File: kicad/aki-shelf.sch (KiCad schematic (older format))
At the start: 39 parts, among them SW1 RESET, SW10 2x2, SW11 2x3, SW12 1x1, SW13 1x2, SW14 1x3, SW2 UPLOAD, SW3 4x1, SW4 4x2, SW5 4x3, SW6 3x1, SW7 3x2, SW8 3x3, SW9 2x1, U1 NJM2884, U2 AE-FT234X, U3 OPA344NA, U4 AQM0802, U5 ESP-WROOM-32

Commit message: 自動配線を適用
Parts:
- LS1: value Speaker -> UGCT7525AN4
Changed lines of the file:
@@
 LIBS:aki-shelf
 LIBS:switches
+LIBS:aki-shelf-cache
 EELAYER 25 0
 EELAYER END
@@
 P 6450 3200
 F 0 "LS1" H 6500 3425 50  0000 R CNN
-F 1 "Speaker" H 6500 3350 50  0000 R CNN
+F 1 "UGCT7525AN4" H 6500 3350 50  0000 R CNN
 F 2 "aki-shelf:UGCT7525AN4" H 6450 3000 50  0001 C CNN
 F 3 "" H 6440 3150 50  0001 C CNN

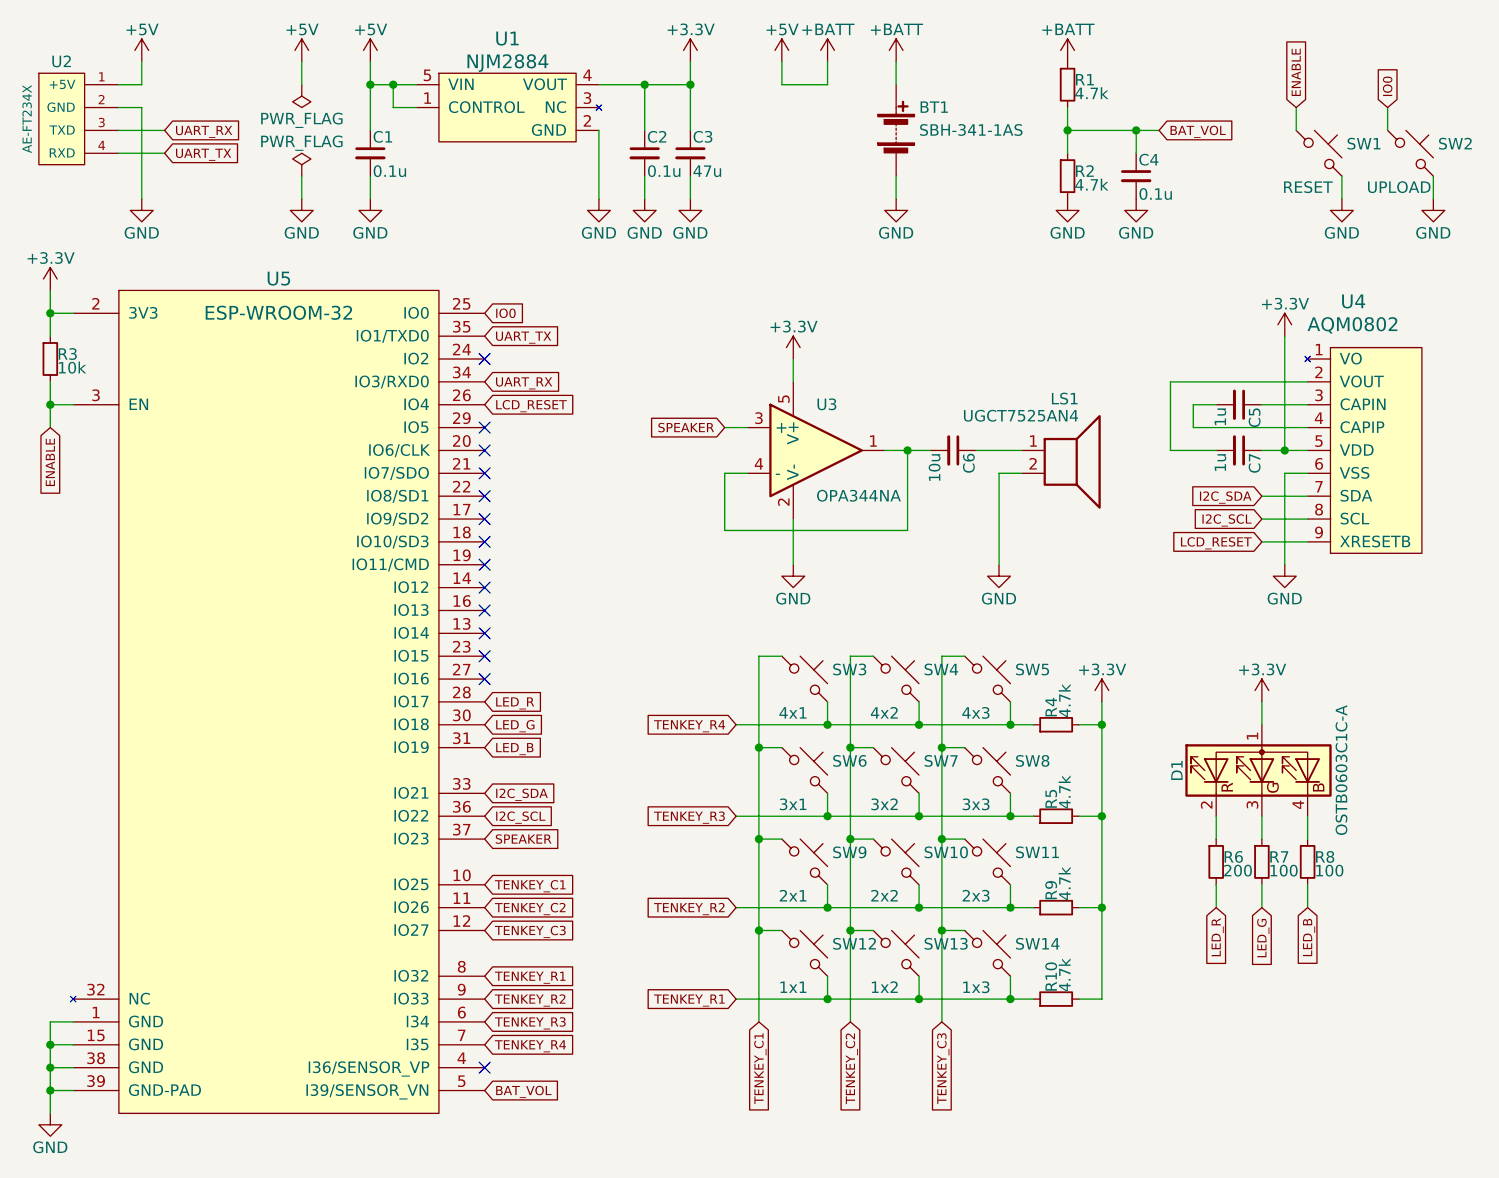
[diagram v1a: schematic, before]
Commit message: 基板を両面にして小型化
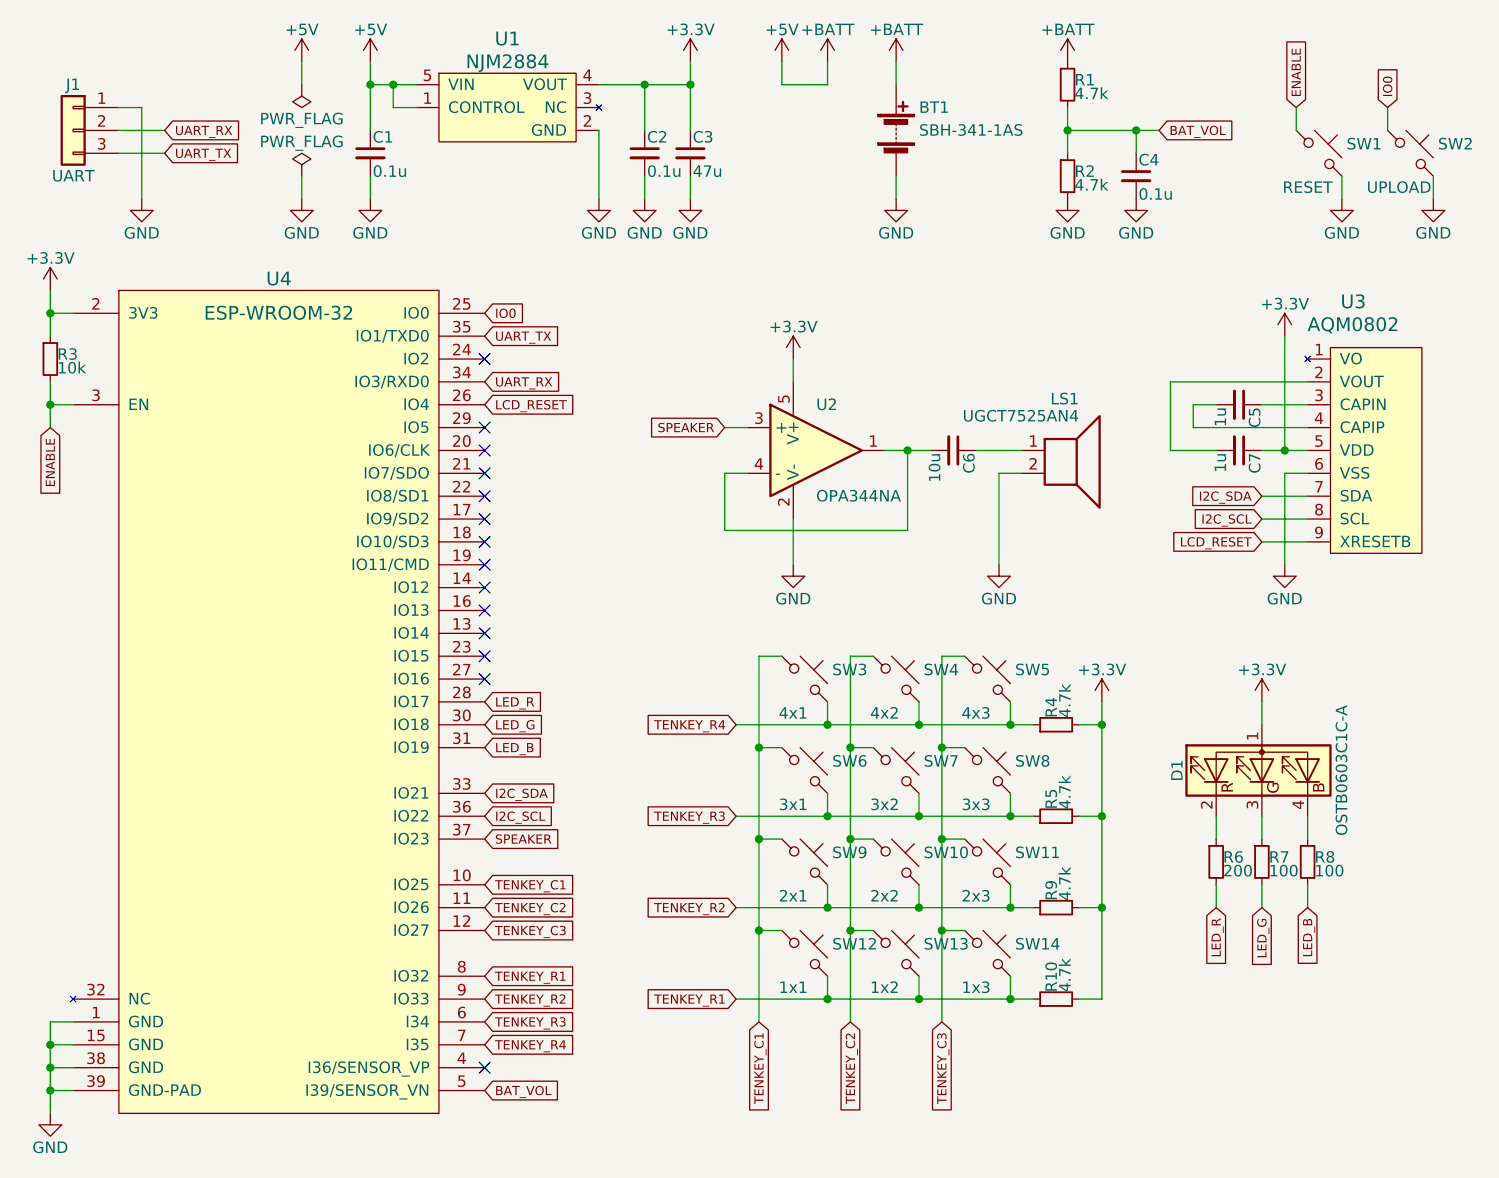
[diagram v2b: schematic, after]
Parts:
- removed U2: AE-FT234X, Pin_Headers:Pin_Header_Straight_1x04_Pitch2.54mm, symbol AE-FT234X
- added J1: UART, Socket_Strips:Socket_Strip_Straight_1x03_Pitch2.54mm, symbol Conn_01x03
- renumbered U3 to U2, U4 to U3, U5 to U4
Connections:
- net GND: now also J1.1 (Pin_1)
- net UART_RX: now also J1.2 (Pin_2)
- net UART_TX: now also J1.3 (Pin_3)
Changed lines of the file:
@@
 	8050 2100 8050 2000
 $Comp
-L OPA340NA U3
+L OPA340NA U2
 U 1 1 5A899835
 P 5350 3200
-F 0 "U3" H 5350 3400 50  0000 L CNN
+F 0 "U2" H 5350 3400 50  0000 L CNN
 F 1 "OPA344NA" H 5350 3000 50  0000 L CNN
 F 2 "TO_SOT_Packages_SMD:SOT-23-5" H 5350 3200 50  0001 C CNN
@@
 $EndComp
 $Comp
-L AQM0802 U4
+L AQM0802 U3
 U 1 1 5A8C4AD2
 P 7700 3200
-F 0 "U4" H 7700 3850 60  0000 C CNN
+F 0 "U3" H 7700 3850 60  0000 C CNN
 F 1 "AQM0802" H 7700 3750 60  0000 C CNN
 F 2 "aki-shelf:AQM0802A-RN-GBW" H 7700 3750 60  0001 C CNN
@@
 $EndComp
 Wire Wire Line
-	2400 1600 2300 1600
-Wire Wire Line
-	2400 1600 2400 1500
-$Comp
-L +5V #PWR022
-U 1 1 58F006DB
-P 2400 1500
-F 0 "#PWR022" H 2400 1350 50  0001 C CNN
-F 1 "+5V" H 2400 1640 50  0000 C CNN
-F 2 "" H 2400 1500 50  0000 C CNN
-F 3 "" H 2400 1500 50  0000 C CNN
-	1    2400 1500
-	1    0    0    -1
-$EndComp
-Wire Wire Line
 	5700 1500 5700 1600
 $Comp
@@
 $EndComp
 $Comp
-L AE-FT234X U2
-U 1 1 5A8AD757
-P 2100 1750
-F 0 "U2" H 2050 2000 50  0000 C CNN
-F 1 "AE-FT234X" V 1900 1750 40  0000 C CNN
-F 2 "Pin_Headers:Pin_Header_Straight_1x04_Pitch2.54mm" H 2100 2200 60  0001 C CNN
-F 3 "" H 2100 2200 60  0000 C CNN
-	1    2100 1750
-	1    0    0    -1
-$EndComp
-$Comp
-L ESP-WROOM-32 U5
+L ESP-WROOM-32 U4
 U 1 1 5A8AD7EC
 P 3000 4000
-F 0 "U5" H 3000 5550 60  0000 C CNN
+F 0 "U4" H 3000 5550 60  0000 C CNN
 F 1 "ESP-WROOM-32" H 3000 5400 60  0000 C CNN
 F 2 "aki-shelf:ESP-WROOM-32" H 3000 5500 60  0001 C CNN
@@
 NoConn ~ 3900 5900
 $Comp
-L PWR_FLAG #FLG023
+L PWR_FLAG #FLG022
 U 1 1 5A8AC441
 P 3100 1600
-F 0 "#FLG023" H 3100 1675 50  0001 C CNN
+F 0 "#FLG022" H 3100 1675 50  0001 C CNN
 F 1 "PWR_FLAG" H 3100 1750 50  0000 C CNN
 F 2 "" H 3100 1600 50  0001 C CNN
@@
 $EndComp
 $Comp
-L +5V #PWR024
+L +5V #PWR023
 U 1 1 5A8AC4CB
 P 3100 1500
-F 0 "#PWR024" H 3100 1350 50  0001 C CNN
+F 0 "#PWR023" H 3100 1350 50  0001 C CNN
 F 1 "+5V" H 3100 1640 50  0000 C CNN
 F 2 "" H 3100 1500 50  0000 C CNN
@@
 	3100 1500 3100 1600
 $Comp
-L GND #PWR025
+L GND #PWR024
 U 1 1 5A8AC606
 P 3100 2100
-F 0 "#PWR025" H 3100 1850 50  0001 C CNN
+F 0 "#PWR024" H 3100 1850 50  0001 C CNN
 F 1 "GND" H 3100 1950 50  0000 C CNN
 F 2 "" H 3100 2100 50  0000 C CNN
@@
 $EndComp
 $Comp
-L PWR_FLAG #FLG026
+L PWR_FLAG #FLG025
 U 1 1 5A8AC689
 P 3100 2000
-F 0 "#FLG026" H 3100 2075 50  0001 C CNN
+F 0 "#FLG025" H 3100 2075 50  0001 C CNN
 F 1 "PWR_FLAG" H 3100 2150 50  0000 C CNN
 F 2 "" H 3100 2000 50  0001 C CNN
@@
 	3100 2000 3100 2100
 $Comp
-L +BATT #PWR027
+L +BATT #PWR026
 U 1 1 5A8B177B
 P 5700 1500
-F 0 "#PWR027" H 5700 1350 50  0001 C CNN
+F 0 "#PWR026" H 5700 1350 50  0001 C CNN
 F 1 "+BATT" H 5700 1640 50  0000 C CNN
 F 2 "" H 5700 1500 50  0001 C CNN
@@
 $EndComp
 $Comp
-L +BATT #PWR028
+L +BATT #PWR027
 U 1 1 5A8B1853
 P 6450 1500
-F 0 "#PWR028" H 6450 1350 50  0001 C CNN
+F 0 "#PWR027" H 6450 1350 50  0001 C CNN
 F 1 "+BATT" H 6450 1640 50  0000 C CNN
 F 2 "" H 6450 1500 50  0001 C CNN
@@
 $EndComp
 $Comp
-L +5V #PWR029
+L +5V #PWR028
 U 1 1 5A8B1ED8
 P 5200 1500
-F 0 "#PWR029" H 5200 1350 50  0001 C CNN
+F 0 "#PWR028" H 5200 1350 50  0001 C CNN
 F 1 "+5V" H 5200 1640 50  0000 C CNN
 F 2 "" H 5200 1500 50  0000 C CNN
@@
 $EndComp
 $Comp
-L +BATT #PWR030
+L +BATT #PWR029
 U 1 1 5A8B1F58
 P 5400 1500
-F 0 "#PWR030" H 5400 1350 50  0001 C CNN
+F 0 "#PWR029" H 5400 1350 50  0001 C CNN
 F 1 "+BATT" H 5400 1640 50  0000 C CNN
 F 2 "" H 5400 1500 50  0001 C CNN
@@
 Wire Wire Line
 	5400 1600 5400 1500
+$Comp
+L Conn_01x03 J1
+U 1 1 5A8E4B4D
+P 2100 1800
+F 0 "J1" H 2100 2000 50  0000 C CNN
+F 1 "UART" H 2100 1600 50  0000 C CNN
+F 2 "Socket_Strips:Socket_Strip_Straight_1x03_Pitch2.54mm" H 2100 1800 50  0001 C CNN
+F 3 "" H 2100 1800 50  0001 C CNN
+	1    2100 1800
+	-1   0    0    -1
+$EndComp
 $EndSCHEMATC

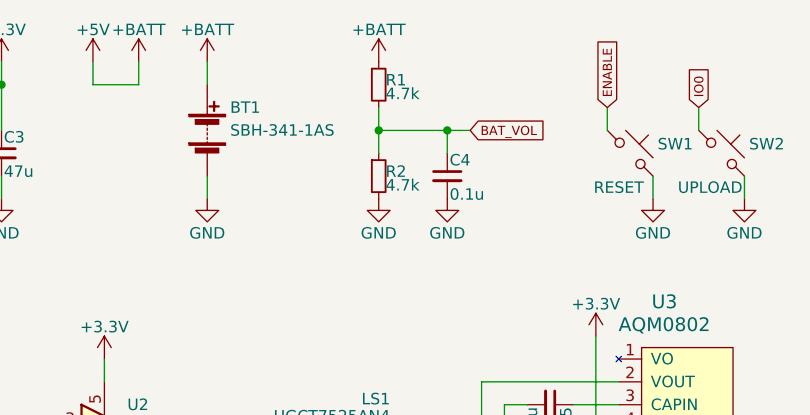
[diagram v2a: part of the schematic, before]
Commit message: 穴径を3mmに変更
貼り付けボスが使えるように
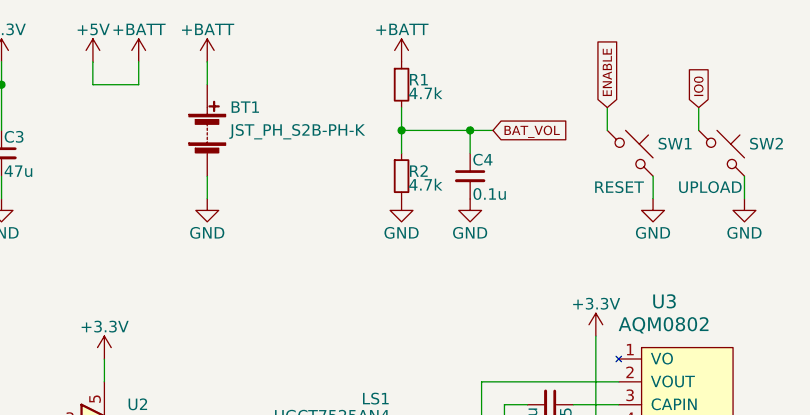
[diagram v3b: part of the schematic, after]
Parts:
- BT1: value SBH-341-1AS -> JST_PH_S2B-PH-K
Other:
- moved on the sheet: C4, R1, R2
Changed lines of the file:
@@
 P 5700 1800
 F 0 "BT1" H 5800 1900 50  0000 L CNN
-F 1 "SBH-341-1AS" H 5800 1800 50  0000 L CNN
+F 1 "JST_PH_S2B-PH-K" H 5800 1800 50  0000 L CNN
 F 2 "Connectors_JST:JST_PH_S2B-PH-K_02x2.00mm_Angled" V 5700 1860 50  0001 C CNN
 F 3 "" V 5700 1860 50  0001 C CNN
@@
 L R_Small R1
 U 1 1 5A8D8861
-P 6450 1600
-F 0 "R1" H 6480 1620 50  0000 L CNN
-F 1 "4.7k" H 6480 1560 50  0000 L CNN
-F 2 "Resistors_SMD:R_0603" H 6450 1600 50  0001 C CNN
-F 3 "" H 6450 1600 50  0001 C CNN
-	1    6450 1600
+P 6550 1600
+F 0 "R1" H 6580 1620 50  0000 L CNN
+F 1 "4.7k" H 6580 1560 50  0000 L CNN
+F 2 "Resistors_SMD:R_0603" H 6550 1600 50  0001 C CNN
+F 3 "" H 6550 1600 50  0001 C CNN
+	1    6550 1600
 	1    0    0    -1
 $EndComp
@@
 L R_Small R2
 U 1 1 5A8D88EB
-P 6450 2000
-F 0 "R2" H 6480 2020 50  0000 L CNN
-F 1 "4.7k" H 6480 1960 50  0000 L CNN
-F 2 "Resistors_SMD:R_0603" H 6450 2000 50  0001 C CNN
-F 3 "" H 6450 2000 50  0001 C CNN
-	1    6450 2000
+P 6550 2000
+F 0 "R2" H 6580 2020 50  0000 L CNN
+F 1 "4.7k" H 6580 1960 50  0000 L CNN
+F 2 "Resistors_SMD:R_0603" H 6550 2000 50  0001 C CNN
+F 3 "" H 6550 2000 50  0001 C CNN
+	1    6550 2000
 	1    0    0    -1
 $EndComp
@@
 L GND #PWR014
 U 1 1 5A8D8D69
-P 6450 2100
-F 0 "#PWR014" H 6450 1850 50  0001 C CNN
-F 1 "GND" H 6450 1950 50  0000 C CNN
-F 2 "" H 6450 2100 50  0000 C CNN
-F 3 "" H 6450 2100 50  0000 C CNN
-	1    6450 2100
+P 6550 2100
+F 0 "#PWR014" H 6550 1850 50  0001 C CNN
+F 1 "GND" H 6550 1950 50  0000 C CNN
+F 2 "" H 6550 2100 50  0000 C CNN
+F 3 "" H 6550 2100 50  0000 C CNN
+	1    6550 2100
 	1    0    0    -1
 $EndComp
@@
 L C_Small C4
 U 1 1 5A8D8E3E
-P 6750 2000
-F 0 "C4" H 6760 2070 50  0000 L CNN
-F 1 "0.1u" H 6760 1920 50  0000 L CNN
-F 2 "Capacitors_SMD:C_0603" H 6750 2000 50  0001 C CNN
-F 3 "" H 6750 2000 50  0001 C CNN
-	1    6750 2000
+P 6850 2000
+F 0 "C4" H 6860 2070 50  0000 L CNN
+F 1 "0.1u" H 6860 1920 50  0000 L CNN
+F 2 "Capacitors_SMD:C_0603" H 6850 2000 50  0001 C CNN
+F 3 "" H 6850 2000 50  0001 C CNN
+	1    6850 2000
 	1    0    0    -1
 $EndComp
@@
 L GND #PWR015
 U 1 1 5A8D8F7F
-P 6750 2100
-F 0 "#PWR015" H 6750 1850 50  0001 C CNN
-F 1 "GND" H 6750 1950 50  0000 C CNN
-F 2 "" H 6750 2100 50  0000 C CNN
-F 3 "" H 6750 2100 50  0000 C CNN
-	1    6750 2100
-	1    0    0    -1
-$EndComp
-Wire Wire Line
-	6750 1900 6750 1800
-Wire Wire Line
-	6450 1800 6850 1800
-Wire Wire Line
-	6450 1700 6450 1900
-Connection ~ 6450 1800
-Text GLabel 6850 1800 2    40   Input ~ 0
+P 6850 2100
+F 0 "#PWR015" H 6850 1850 50  0001 C CNN
+F 1 "GND" H 6850 1950 50  0000 C CNN
+F 2 "" H 6850 2100 50  0000 C CNN
+F 3 "" H 6850 2100 50  0000 C CNN
+	1    6850 2100
+	1    0    0    -1
+$EndComp
+Wire Wire Line
+	6850 1900 6850 1800
+Wire Wire Line
+	6550 1800 6950 1800
+Wire Wire Line
+	6550 1700 6550 1900
+Connection ~ 6550 1800
+Text GLabel 6950 1800 2    40   Input ~ 0
 BAT_VOL
-Connection ~ 6750 1800
+Connection ~ 6850 1800
 Wire Wire Line
 	3400 2000 3400 2100
@@
 L +BATT #PWR027
 U 1 1 5A8B1853
-P 6450 1500
-F 0 "#PWR027" H 6450 1350 50  0001 C CNN
-F 1 "+BATT" H 6450 1640 50  0000 C CNN
-F 2 "" H 6450 1500 50  0001 C CNN
-F 3 "" H 6450 1500 50  0001 C CNN
-	1    6450 1500
-	1    0    0    -1
-$EndComp
+P 6550 1500
+F 0 "#PWR027" H 6550 1350 50  0001 C CNN
+F 1 "+BATT" H 6550 1640 50  0000 C CNN
+F 2 "" H 6550 1500 50  0001 C CNN
+F 3 "" H 6550 1500 50  0001 C CNN
+	1    6550 1500
+	1    0    0    -1
+$EndComp

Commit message: 基板を改良
スイッチの位置，スピーカーの回路など
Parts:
- removed C6: 10u, Capacitors_SMD:C_0805, symbol C_Small
- removed D1: OSTB0603C1C-A, aki-shelf:OSTB0603C1C-A, symbol LED_ARGB
- removed U2: OPA344NA, TO_SOT_Packages_SMD:SOT-23-5, symbol OPA340NA
- added C7: 0.1u, Capacitors_SMD:C_0603, symbol C_Small
- added D1: OSTB0603C1C-A, aki-shelf:OSTB0603C1C-A, symbol OSTB0603C1C-A
- added Q1: BSS138, TO_SOT_Packages_SMD:SOT-23, symbol Q_NMOS_GSD
- added R4: 100k, Resistors_SMD:R_0603, symbol R_Small
- R3: value 10k -> 4.7k
- renumbered C7 to C6, R9 to R10, R10 to R11, R4 to R5, R5 to R6, R6 to R7, R7 to R8, R8 to R9, U3 to U2, U4 to U3
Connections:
- net +3V3: now also LS1.1, D1.1 (A)
- net GND: now also Q1.2 (S), R4.2; no longer LS1.2
- net SPEAKER: now also C7.2
- net at R7.1: now also D1.2 (RK)
- net at R8.1: now also D1.3 (GK)
- net at R9.1: now also D1.4 (BK)
- new net: LS1.2, Q1.3 (D)
- new net: C7.1, Q1.1 (G), R4.1
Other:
- moved on the sheet: LS1
